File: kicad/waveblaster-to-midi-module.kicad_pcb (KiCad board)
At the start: 2 copper layers, 33 x 94.5 mm, 14 parts, among them J1 Midi Out, J2 Midi In, J3 Right In, J4 Left In, J5 Right Out, J6 Left Out, J7 Wavetable Input, U1 H11L1

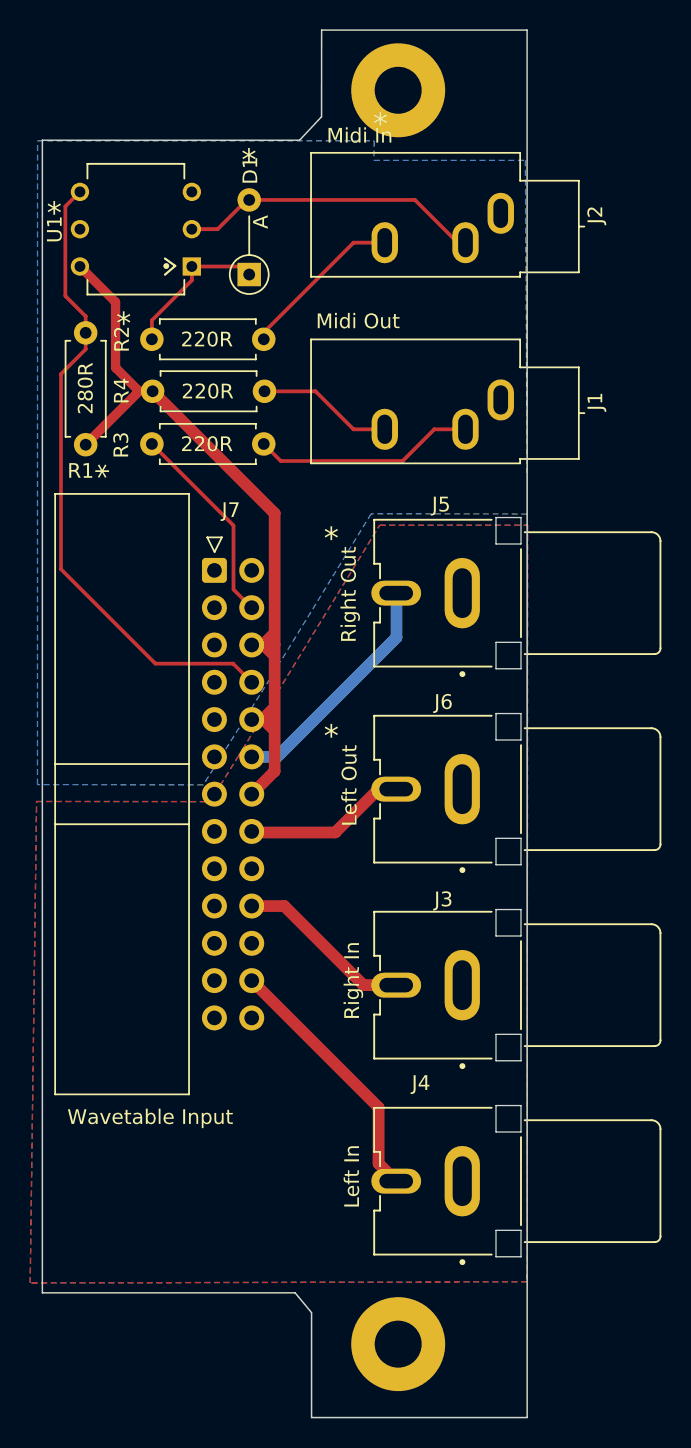
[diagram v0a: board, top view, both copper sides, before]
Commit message: v2.0: low profile
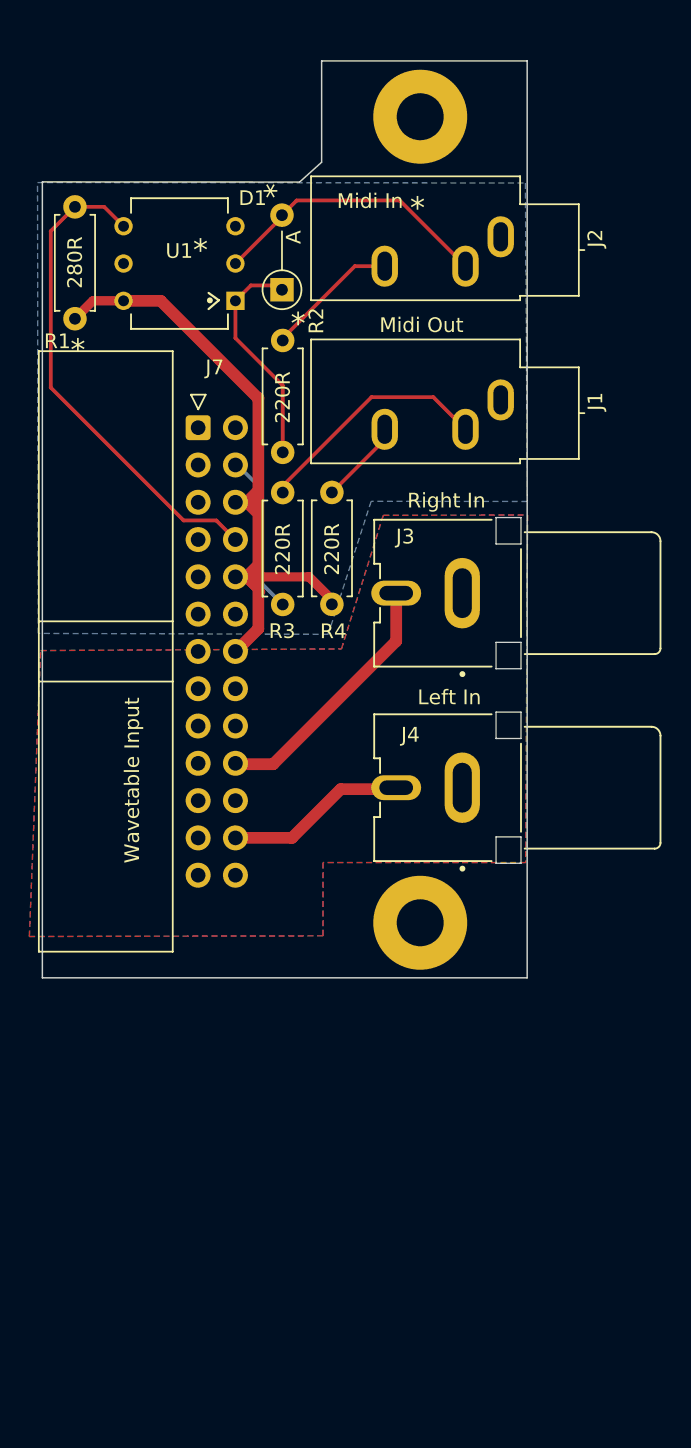
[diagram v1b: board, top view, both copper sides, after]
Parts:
- removed J5: Right Out, Library:CUI_RCJ-04X
- removed J6: Left Out, Library:CUI_RCJ-043
- moved J4 26.8 mm to (189.6, 104.6)
- moved J3 26.7 mm to (189.6, 91.3)
- moved R4 19.0 mm to (176.7, 92.1), turned to 90 degrees
- moved R3 14.1 mm to (173.3, 92.1), turned to 90 degrees
- moved R2 11.8 mm to (173.3, 81.8), turned to 90 degrees
- moved J7 9.78 mm to (167.6, 80.1)
- moved R1 8.61 mm to (159.2, 72.7)
- moved U1 3.78 mm to (166.4, 68.9)
- moved D1 2.46 mm to (173.3, 70.7)
- moved H1 2.34 mm to (182.7, 58.9)
- moved J2 1.60 mm to (188.2, 67.1)
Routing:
- net WT_AUDIO_R_IN: track 16.3 -> 0.00 mm
- net WT_AUDIO_L_IN: track 11.1 -> 0.00 mm
- net WT_RX: track 43.6 -> 33.7 mm
- net +5V: track 57.7 -> 50.3 mm
- net WT_AUDIO_R_OUT: track 11.8 -> 17.7 mm
- net WT_AUDIO_L_OUT: track 18.0 -> 12.3 mm
- net Net-(D1-Pad1): track 10.2 -> 15.0 mm
- net Net-(J1-PadR): track 9.26 -> 5.29 mm
- net WT_TX: track 14.0 -> 10.9 mm
- net Net-(J2-PadR): track 11.2 -> 8.98 mm
- net Net-(J1-PadT): track 14.2 -> 16.3 mm
- net Net-(D1-Pad2): track 20.7 -> 19.4 mm
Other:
- board size 33 x 94.5 mm -> 33 x 62.4 mm
- board text added: "Waveblaster Breakout Card v2.0 by Nikitalita"
- board text removed: "Waveblaster Breakout Card v1.1 by Nikitalita"
